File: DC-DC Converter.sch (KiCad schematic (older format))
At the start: 4 parts

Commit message: Added libraries used in the project. Top level connections.
Added libraries used in this project to the project folder.

Made additonal top level connections on the top level schematic.
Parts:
- removed L?: 13R106C, digikey-footprints:Inductor_13R106C, symbol dk_Fixed-Inductors:13R106C
- added L?: TCK-154, TCK154, symbol SamacSys_Parts:TCK-154
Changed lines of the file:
@@
-$EndComp
-$Comp
-L dk_Fixed-Inductors:13R106C L?
-U 1 1 5F8D7730
-P 3250 3600
-F 0 "L?" H 3250 3380 60  0000 C CNN
-F 1 "13R106C" H 3250 3486 60  0000 C CNN
-F 2 "digikey-footprints:Inductor_13R106C" H 3450 3800 60  0001 L CNN
-F 3 "https://www.murata-ps.com/data/magnetics/kmp_1300r.pdf" H 3450 3900 60  0001 L CNN
-F 4 "811-2058-ND" H 3450 4000 60  0001 L CNN "Digi-Key_PN"
-F 5 "13R106C" H 3450 4100 60  0001 L CNN "MPN"
-F 6 "Inductors, Coils, Chokes" H 3450 4200 60  0001 L CNN "Category"
-F 7 "Fixed Inductors" H 3450 4300 60  0001 L CNN "Family"
-F 8 "https://www.murata-ps.com/data/magnetics/kmp_1300r.pdf" H 3450 4400 60  0001 L CNN "DK_Datasheet_Link"
-F 9 "/product-detail/en/murata-power-solutions-inc/13R106C/811-2058-ND/1998245" H 3450 4500 60  0001 L CNN "DK_Detail_Page"
-F 10 "FIXED IND 10MH 85MA 23.8 OHM TH" H 3450 4600 60  0001 L CNN "Description"
-F 11 "Murata Power Solutions Inc." H 3450 4700 60  0001 L CNN "Manufacturer"
-F 12 "Active" H 3450 4800 60  0001 L CNN "Status"
-	1    3250 3600
-	-1   0    0    1
 $EndComp
 $Comp
@@
 Connection ~ 4350 4000
 Wire Wire Line
-	3450 3600 3700 3600
-Connection ~ 3700 3600
-Wire Wire Line
-	3050 3600 2750 3600
-Wire Wire Line
 	2750 3900 2750 4000
 Wire Wire Line
@@
 Wire Wire Line
 	2550 3600 2750 3600
+$Comp
+L SamacSys_Parts:TCK-154 L?
+U 1 1 5F89924C
+P 2850 3600
+F 0 "L?" H 3250 3825 50  0000 C CNN
+F 1 "TCK-154" H 3250 3734 50  0000 C CNN
+F 2 "TCK154" H 3500 3650 50  0001 L CNN
+F 3 "https://componentsearchengine.com/Datasheets/1/TCK-154.pdf" H 3500 3550 50  0001 L CNN
+F 4 "Fixed Inductors" H 3500 3450 50  0001 L CNN "Description"
+F 5 "3.7" H 3500 3350 50  0001 L CNN "Height"
+F 6 "495-TCK-154" H 3500 3250 50  0001 L CNN "Mouser Part Number"
+F 7 "https://www.mouser.co.uk/ProductDetail/TRACO-Power/TCK-154?qs=w%2Fv1CP2dgqrcxTwKbnHwhQ%3D%3D" H 3500 3150 50  0001 L CNN "Mouser Price/Stock"
+F 8 "Traco Power" H 3500 3050 50  0001 L CNN "Manufacturer_Name"
+F 9 "TCK-154" H 3500 2950 50  0001 L CNN "Manufacturer_Part_Number"
+	1    2850 3600
+	1    0    0    -1
+$EndComp
+Wire Wire Line
+	3650 3600 3700 3600
+Connection ~ 3700 3600
+Wire Wire Line
+	2850 3600 2750 3600
 Connection ~ 2750 3600
 $EndSCHEMATC

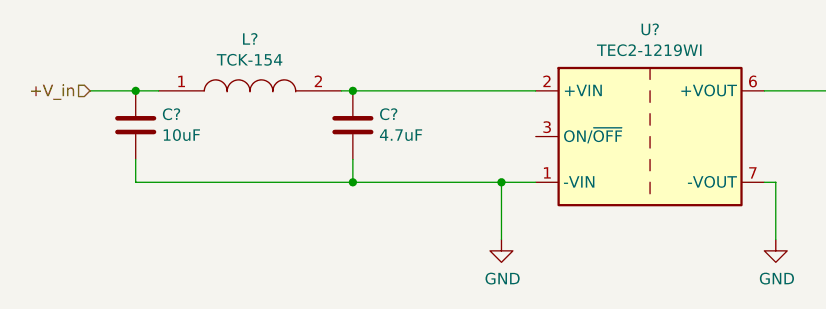
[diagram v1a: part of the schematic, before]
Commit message: Annotated schematics and added UART Jumpers
Annotated schematics.

Added jumpers to GPS UART because I'm still not 100% sure on the connections and I don't want to have to respin a board because I was wrong.
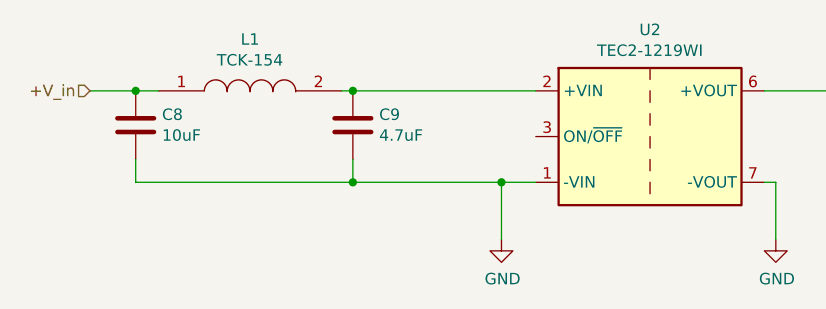
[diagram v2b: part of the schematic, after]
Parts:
- gave numbers to parts that had none: 4
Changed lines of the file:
@@
 	5850 3600 5500 3600
 $Comp
-L Converter_DCDC:TEC2-1219WI U?
+L Converter_DCDC:TEC2-1219WI U2
 U 1 1 5F8D2C7F
 P 5000 3800
-F 0 "U?" H 5000 4267 50  0000 C CNN
+F 0 "U2" H 5000 4267 50  0000 C CNN
 F 1 "TEC2-1219WI" H 5000 4176 50  0000 C CNN
 F 2 "Converter_DCDC:Converter_DCDC_TRACO_TMR-xxxx_THT" H 5000 3450 50  0001 C CNN
@@
 $EndComp
 $Comp
-L Device:C C?
+L Device:C C8
 U 1 1 5F8D9973
 P 2750 3750
-F 0 "C?" H 2865 3796 50  0000 L CNN
+F 0 "C8" H 2865 3796 50  0000 L CNN
 F 1 "10uF" H 2865 3705 50  0000 L CNN
 F 2 "Capacitor_SMD:C_1206_3216Metric_Pad1.33x1.80mm_HandSolder" H 2788 3600 50  0001 C CNN
@@
 $EndComp
 $Comp
-L Device:C C?
+L Device:C C9
 U 1 1 5F8DA48B
 P 3700 3750
-F 0 "C?" H 3815 3796 50  0000 L CNN
+F 0 "C9" H 3815 3796 50  0000 L CNN
 F 1 "4.7uF" H 3815 3705 50  0000 L CNN
 F 2 "Capacitor_SMD:C_1206_3216Metric_Pad1.33x1.80mm_HandSolder" H 3738 3600 50  0001 C CNN
@@
 $EndComp
 $Comp
-L power:GND #PWR?
+L power:GND #PWR011
 U 1 1 5F8DA63B
 P 4350 4250
-F 0 "#PWR?" H 4350 4000 50  0001 C CNN
+F 0 "#PWR011" H 4350 4000 50  0001 C CNN
 F 1 "GND" H 4355 4077 50  0000 C CNN
 F 2 "" H 4350 4250 50  0001 C CNN
@@
 $EndComp
 $Comp
-L power:GND #PWR?
+L power:GND #PWR012
 U 1 1 5F8DAAC8
 P 5550 4250
-F 0 "#PWR?" H 5550 4000 50  0001 C CNN
+F 0 "#PWR012" H 5550 4000 50  0001 C CNN
 F 1 "GND" H 5555 4077 50  0000 C CNN
 F 2 "" H 5550 4250 50  0001 C CNN
@@
 	2550 3600 2750 3600
 $Comp
-L SamacSys_Parts:TCK-154 L?
+L SamacSys_Parts:TCK-154 L1
 U 1 1 5F89924C
 P 2850 3600
-F 0 "L?" H 3250 3825 50  0000 C CNN
+F 0 "L1" H 3250 3825 50  0000 C CNN
 F 1 "TCK-154" H 3250 3734 50  0000 C CNN
 F 2 "TCK154" H 3500 3650 50  0001 L CNN

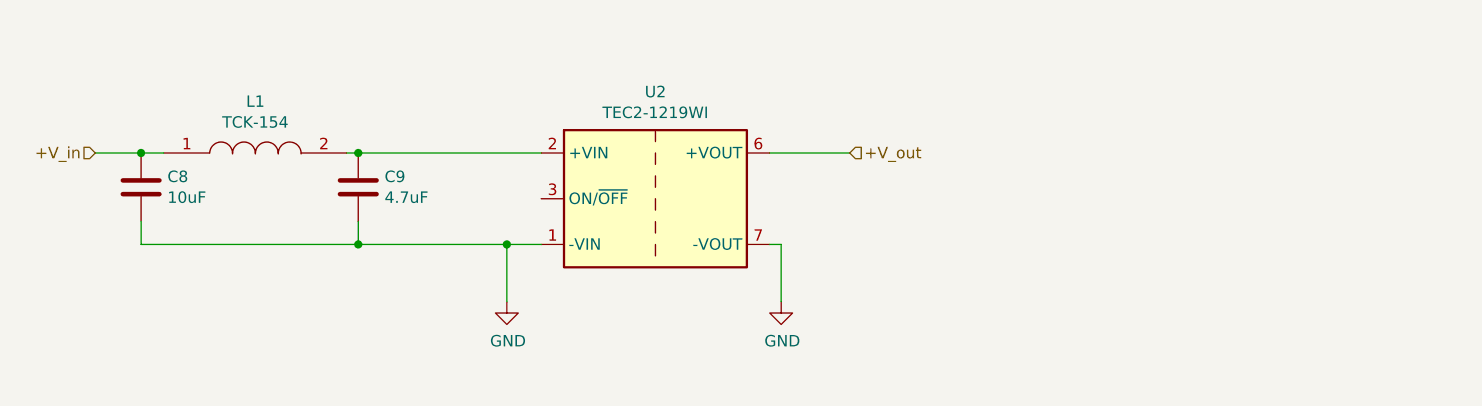
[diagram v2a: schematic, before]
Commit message: eFuse added
Added eFuse, LEDs, and addtional power configuration options.
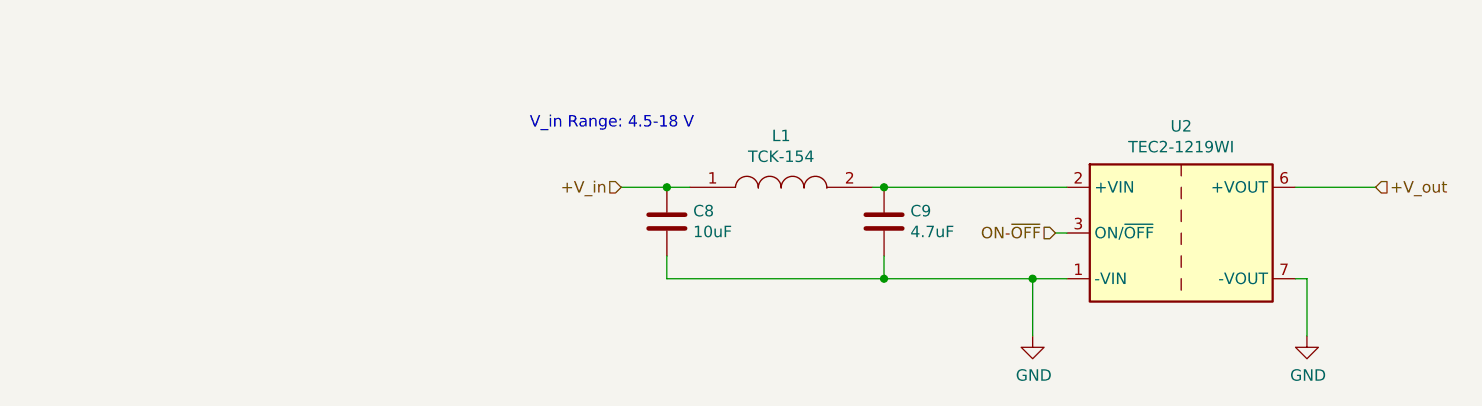
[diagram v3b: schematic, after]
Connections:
- net ON-~OFF: now reaches U2.3 (ON/~OFF)
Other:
- note added: "V_in Range: 4.5-18 V"
- moved on the sheet: C8, C9, L1, U2
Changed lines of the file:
@@
 $Descr A4 11693 8268
 encoding utf-8
-Sheet 4 4
-Title ""
-Date ""
-Rev ""
+Sheet 3 5
+Title "DC-DC Converter"
+Date "2020-10-17"
+Rev "2"
 Comp ""
 Comment1 ""
@@
 $EndDescr
 Wire Wire Line
-	4500 4000 4350 4000
+	6800 4150 6650 4150
 Wire Wire Line
-	5500 4000 5550 4000
-Text HLabel 2550 3600 0    50   Input ~ 0
+	7800 4150 7850 4150
+Text HLabel 4850 3750 0    50   Input ~ 0
 +V_in
-Text HLabel 5850 3600 2    50   Input ~ 0
+Text HLabel 8150 3750 2    50   Input ~ 0
 +V_out
 Wire Wire Line
-	5850 3600 5500 3600
+	8150 3750 7800 3750
 $Comp
 L Converter_DCDC:TEC2-1219WI U2
 U 1 1 5F8D2C7F
-P 5000 3800
-F 0 "U2" H 5000 4267 50  0000 C CNN
-F 1 "TEC2-1219WI" H 5000 4176 50  0000 C CNN
-F 2 "Converter_DCDC:Converter_DCDC_TRACO_TMR-xxxx_THT" H 5000 3450 50  0001 C CNN
-F 3 "https://www.tracopower.com/products/tec2wi.pdf" H 5000 3300 50  0001 C CNN
-	1    5000 3800
+P 7300 3950
+F 0 "U2" H 7300 4417 50  0000 C CNN
+F 1 "TEC2-1219WI" H 7300 4326 50  0000 C CNN
+F 2 "Converter_DCDC:Converter_DCDC_TRACO_TMR-xxxx_THT" H 7300 3600 50  0001 C CNN
+F 3 "https://www.tracopower.com/products/tec2wi.pdf" H 7300 3450 50  0001 C CNN
+	1    7300 3950
 	1    0    0    -1
 $EndComp
@@
 L Device:C C8
 U 1 1 5F8D9973
-P 2750 3750
-F 0 "C8" H 2865 3796 50  0000 L CNN
-F 1 "10uF" H 2865 3705 50  0000 L CNN
-F 2 "Capacitor_SMD:C_1206_3216Metric_Pad1.33x1.80mm_HandSolder" H 2788 3600 50  0001 C CNN
-F 3 "https://media.digikey.com/pdf/Data%20Sheets/Samsung%20PDFs/CL_Series_MLCC_ds.pdf" H 2750 3750 50  0001 C CNN
-F 4 "Samsung Electro-Mechanics" H 2750 3750 50  0001 C CNN "Manufacturer"
-F 5 "CL31A106KAHNNNE" H 2750 3750 50  0001 C CNN "MPN"
-	1    2750 3750
+P 5050 3900
+F 0 "C8" H 5165 3946 50  0000 L CNN
+F 1 "10uF" H 5165 3855 50  0000 L CNN
+F 2 "Capacitor_SMD:C_1206_3216Metric_Pad1.33x1.80mm_HandSolder" H 5088 3750 50  0001 C CNN
+F 3 "https://media.digikey.com/pdf/Data%20Sheets/Samsung%20PDFs/CL_Series_MLCC_ds.pdf" H 5050 3900 50  0001 C CNN
+F 4 "Samsung Electro-Mechanics" H 5050 3900 50  0001 C CNN "Manufacturer"
+F 5 "CL31A106KAHNNNE" H 5050 3900 50  0001 C CNN "MPN"
+	1    5050 3900
 	1    0    0    -1
 $EndComp
@@
 L Device:C C9
 U 1 1 5F8DA48B
-P 3700 3750
-F 0 "C9" H 3815 3796 50  0000 L CNN
-F 1 "4.7uF" H 3815 3705 50  0000 L CNN
-F 2 "Capacitor_SMD:C_1206_3216Metric_Pad1.33x1.80mm_HandSolder" H 3738 3600 50  0001 C CNN
-F 3 "https://product.tdk.com/info/en/catalog/datasheets/mlcc_commercial_general_en.pdf?ref_disty=digikey" H 3700 3750 50  0001 C CNN
-F 4 "TDK Corporation" H 3700 3750 50  0001 C CNN "Manufacturer"
-F 5 "C3216X7R1E475K160AC" H 3700 3750 50  0001 C CNN "MPN"
-	1    3700 3750
+P 6000 3900
+F 0 "C9" H 6115 3946 50  0000 L CNN
+F 1 "4.7uF" H 6115 3855 50  0000 L CNN
+F 2 "Capacitor_SMD:C_1206_3216Metric_Pad1.33x1.80mm_HandSolder" H 6038 3750 50  0001 C CNN
+F 3 "https://product.tdk.com/info/en/catalog/datasheets/mlcc_commercial_general_en.pdf?ref_disty=digikey" H 6000 3900 50  0001 C CNN
+F 4 "TDK Corporation" H 6000 3900 50  0001 C CNN "Manufacturer"
+F 5 "C3216X7R1E475K160AC" H 6000 3900 50  0001 C CNN "MPN"
+	1    6000 3900
 	1    0    0    -1
 $EndComp
@@
 L power:GND #PWR011
 U 1 1 5F8DA63B
-P 4350 4250
-F 0 "#PWR011" H 4350 4000 50  0001 C CNN
-F 1 "GND" H 4355 4077 50  0000 C CNN
-F 2 "" H 4350 4250 50  0001 C CNN
-F 3 "" H 4350 4250 50  0001 C CNN
-	1    4350 4250
+P 6650 4400
+F 0 "#PWR011" H 6650 4150 50  0001 C CNN
+F 1 "GND" H 6655 4227 50  0000 C CNN
+F 2 "" H 6650 4400 50  0001 C CNN
+F 3 "" H 6650 4400 50  0001 C CNN
+	1    6650 4400
 	1    0    0    -1
 $EndComp
@@
 L power:GND #PWR012
 U 1 1 5F8DAAC8
-P 5550 4250
-F 0 "#PWR012" H 5550 4000 50  0001 C CNN
-F 1 "GND" H 5555 4077 50  0000 C CNN
-F 2 "" H 5550 4250 50  0001 C CNN
-F 3 "" H 5550 4250 50  0001 C CNN
-	1    5550 4250
+P 7850 4400
+F 0 "#PWR012" H 7850 4150 50  0001 C CNN
+F 1 "GND" H 7855 4227 50  0000 C CNN
+F 2 "" H 7850 4400 50  0001 C CNN
+F 3 "" H 7850 4400 50  0001 C CNN
+	1    7850 4400
 	1    0    0    -1
 $EndComp
 Wire Wire Line
-	4350 4000 4350 4250
+	6650 4150 6650 4400
 Wire Wire Line
-	5550 4000 5550 4250
+	7850 4150 7850 4400
 Wire Wire Line
-	3700 3600 4500 3600
+	6000 3750 6800 3750
 Wire Wire Line
-	3700 3900 3700 4000
+	6000 4050 6000 4150
 Wire Wire Line
-	3700 4000 4350 4000
-Connection ~ 4350 4000
+	6000 4150 6650 4150
+Connection ~ 6650 4150
 Wire Wire Line
-	2750 3900 2750 4000
+	5050 4050 5050 4150
 Wire Wire Line
-	2750 4000 3700 4000
-Connection ~ 3700 4000
+	5050 4150 6000 4150
+Connection ~ 6000 4150
 Wire Wire Line
-	2550 3600 2750 3600
+	4850 3750 5050 3750
 $Comp
 L SamacSys_Parts:TCK-154 L1
 U 1 1 5F89924C
-P 2850 3600
-F 0 "L1" H 3250 3825 50  0000 C CNN
-F 1 "TCK-154" H 3250 3734 50  0000 C CNN
-F 2 "TCK154" H 3500 3650 50  0001 L CNN
-F 3 "https://componentsearchengine.com/Datasheets/1/TCK-154.pdf" H 3500 3550 50  0001 L CNN
-F 4 "Fixed Inductors" H 3500 3450 50  0001 L CNN "Description"
-F 5 "3.7" H 3500 3350 50  0001 L CNN "Height"
-F 6 "495-TCK-154" H 3500 3250 50  0001 L CNN "Mouser Part Number"
-F 7 "https://www.mouser.co.uk/ProductDetail/TRACO-Power/TCK-154?qs=w%2Fv1CP2dgqrcxTwKbnHwhQ%3D%3D" H 3500 3150 50  0001 L CNN "Mouser Price/Stock"
-F 8 "Traco Power" H 3500 3050 50  0001 L CNN "Manufacturer_Name"
-F 9 "TCK-154" H 3500 2950 50  0001 L CNN "Manufacturer_Part_Number"
-	1    2850 3600
+P 5150 3750
+F 0 "L1" H 5550 3975 50  0000 C CNN
+F 1 "TCK-154" H 5550 3884 50  0000 C CNN
+F 2 "TCK154" H 5800 3800 50  0001 L CNN
+F 3 "https://componentsearchengine.com/Datasheets/1/TCK-154.pdf" H 5800 3700 50  0001 L CNN
+F 4 "Fixed Inductors" H 5800 3600 50  0001 L CNN "Description"
+F 5 "3.7" H 5800 3500 50  0001 L CNN "Height"
+F 6 "495-TCK-154" H 5800 3400 50  0001 L CNN "Mouser Part Number"
+F 7 "https://www.mouser.co.uk/ProductDetail/TRACO-Power/TCK-154?qs=w%2Fv1CP2dgqrcxTwKbnHwhQ%3D%3D" H 5800 3300 50  0001 L CNN "Mouser Price/Stock"
+F 8 "Traco Power" H 5800 3200 50  0001 L CNN "Manufacturer_Name"
+F 9 "TCK-154" H 5800 3100 50  0001 L CNN "Manufacturer_Part_Number"
+	1    5150 3750
 	1    0    0    -1
 $EndComp
 Wire Wire Line
-	3650 3600 3700 3600
-Connection ~ 3700 3600
+	5950 3750 6000 3750
+Connection ~ 6000 3750
 Wire Wire Line
-	2850 3600 2750 3600
-Connection ~ 2750 3600
+	5150 3750 5050 3750
+Connection ~ 5050 3750
+Text Notes 4450 3500 0    50   ~ 0
+V_in Range: 4.5-18 V
+Text HLabel 6750 3950 0    50   Input ~ 0
+ON-~OFF
+Wire Wire Line
+	6750 3950 6800 3950
 $EndSCHEMATC
